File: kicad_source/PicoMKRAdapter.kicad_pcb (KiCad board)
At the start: 2 copper layers, 51 x 27 mm, 5 parts, among them CN1 RASPBERRYPI_PICO, CN2 ARDUINO_MKR, CN3 CONN_01X04

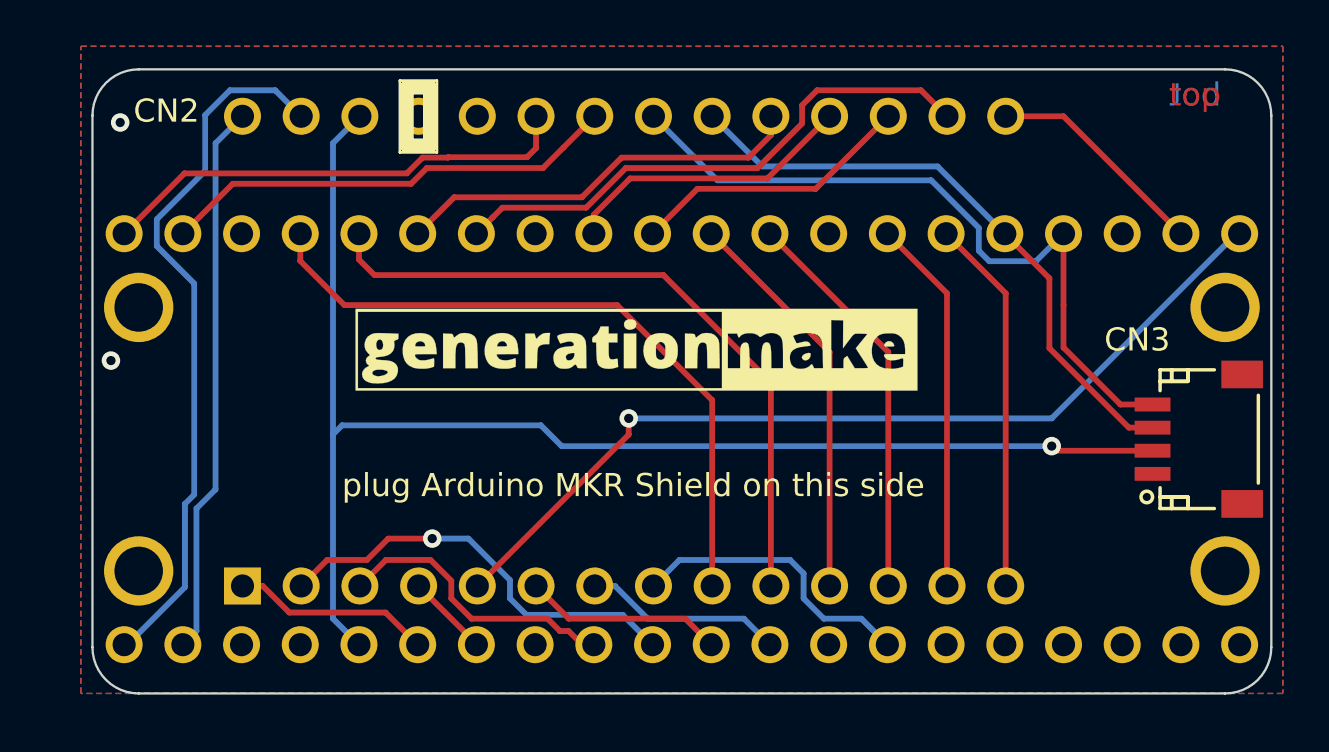
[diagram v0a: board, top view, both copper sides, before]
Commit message: updated layout and schematic, added i2c and serial connectors
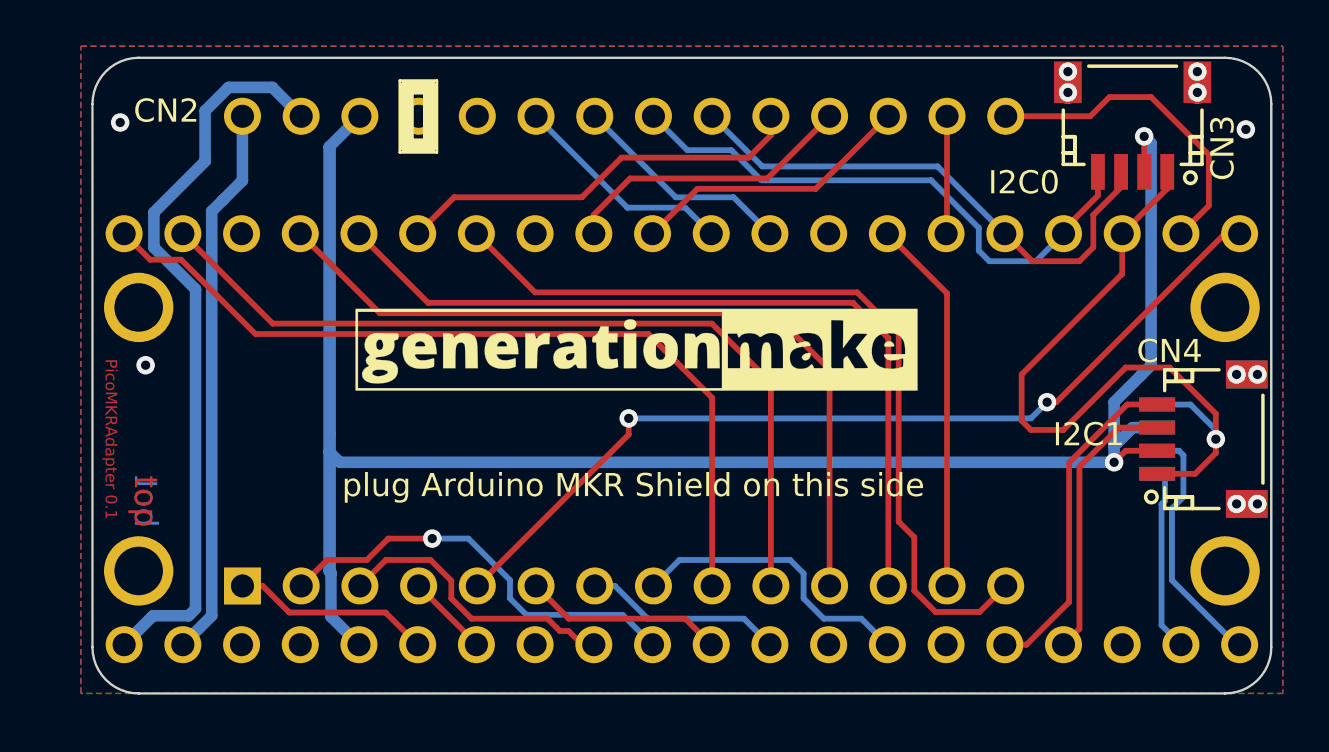
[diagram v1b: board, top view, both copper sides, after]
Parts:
- added CN4: CONN_01X04, connectors_JST_SH:Connectors_JST_SM04B-SRSS-TB, F.Cu at (202.5, 100.0)
- added CN5: CONN_01X04, connectors_JST_SH:Connectors_JST_SM04B-SRSS-TB, B.Cu at (202.5, 100.0)
- moved CN3 13.8 mm to (199.5, 86.5), turned to 180 degrees
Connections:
- net /SCL renamed /I2C0_SCL
- net /SDA renamed /I2C0_SDA
- CN1 pad 1: /TX -> /0
- CN1 pad 11: /2 -> /UART1_TX
- CN1 pad 12: /3 -> /UART1_RX
- CN1 pad 15: /5 -> /7
- CN1 pad 2: /RX -> /1
- CN1 pad 21: (no net) -> /UART0_TX
- CN1 pad 22: (no net) -> /UART0_RX
- CN1 pad 24: (no net) -> /I2C1_SDA
- CN1 pad 25: (no net) -> /I2C1_SCL
- CN1 pad 4: /0 -> /2
- CN1 pad 5: /1 -> /3
- CN1 pad 7: /7 -> /5
- CN2 pad 22: /RX -> /UART1_RX
- CN2 pad 23: /TX -> /UART1_TX
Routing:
- net +3V3: track 59.9 -> 102.6 mm, vias 1 -> 2
- net GND: track 0.00 -> 31.9 mm, vias 2 -> 4
- net /TX: track 20.7 -> 0.00 mm
- net /5: track 16.3 -> 36.3 mm
- net /RX: track 19.9 -> 0.00 mm
- net /7: track 23.9 -> 5.10 mm
- net /3: track 17.4 -> 35.5 mm
- net /2: track 17.4 -> 34.7 mm
- net /I2C1_SCL: track 0.00 -> 14.4 mm
- net /I2C1_SDA: track 0.00 -> 12.0 mm
- net /UART0_TX: track 0.00 -> 10.9 mm
- net /UART1_TX: track 0.00 -> 9.68 mm
- net /UART1_RX: track 0.00 -> 9.68 mm
- net /UART0_RX: track 0.00 -> 8.14 mm
- net /0: track 29.5 -> 36.5 mm
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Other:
- board size 51 x 27 mm -> 51 x 27.5 mm
- board text added: "I2C0"
- board text added: "I2C1"
- board text added: "PicoMKRAdapter 0.1"
- board text added: "UART0"

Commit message: updated pico footprint
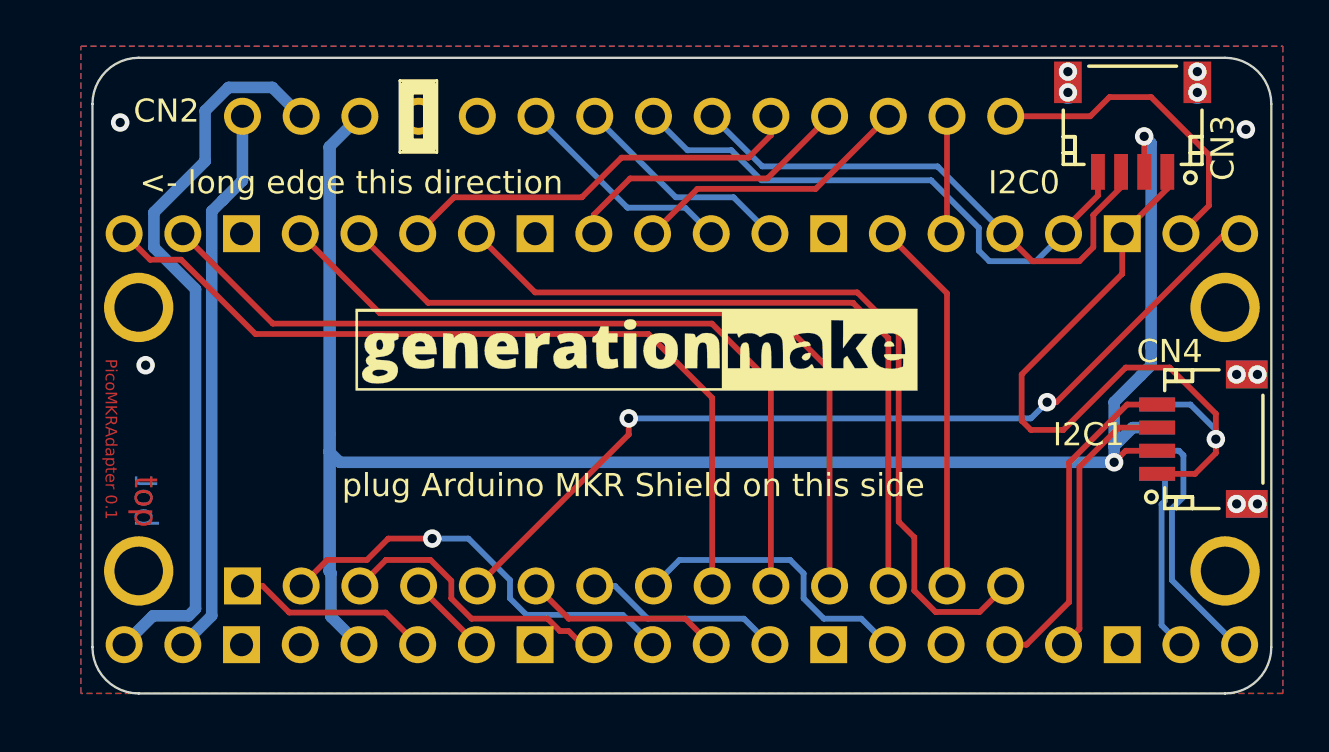
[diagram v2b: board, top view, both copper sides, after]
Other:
- board text added: "<- long edge this direction"
- board text added: "plug Rasperry Pi Pico on this side USB this direction ->"
- board text removed: "plug Rasperry Pi Pico on this side"

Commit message: connected RUN to RESET, added some labels
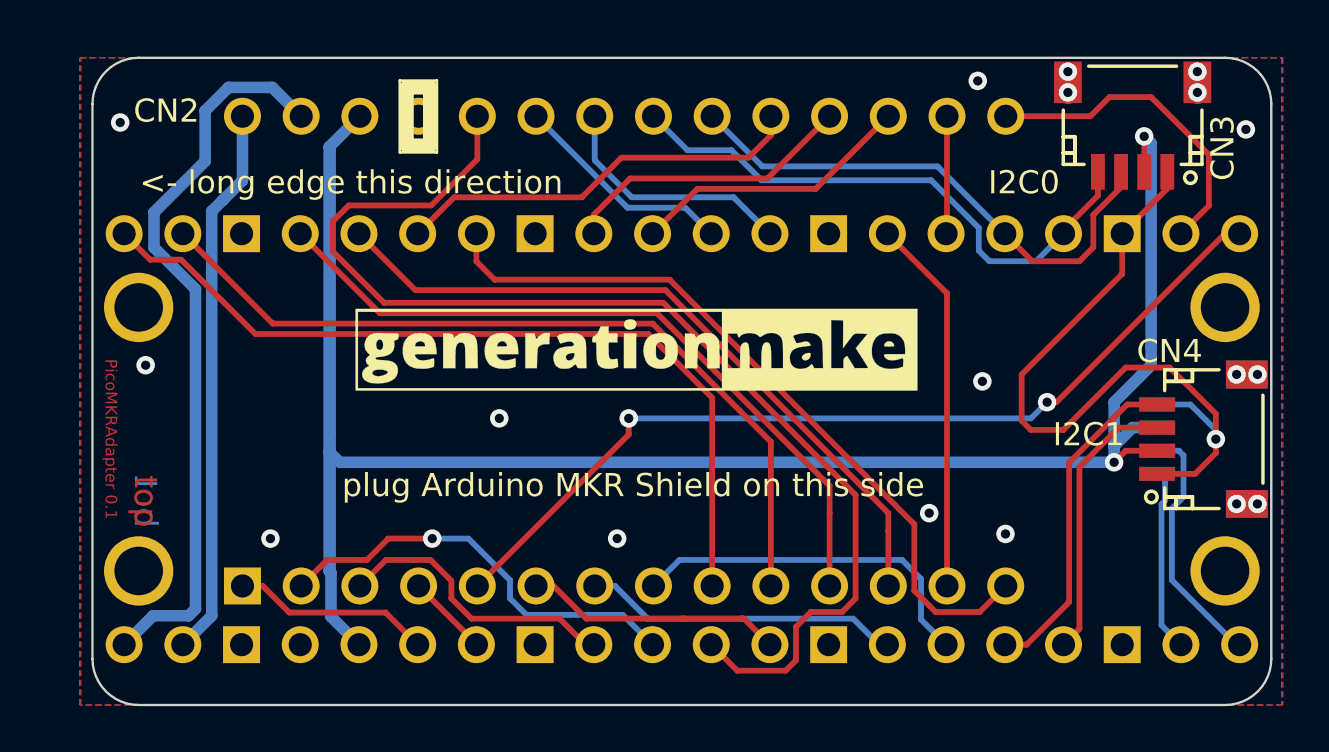
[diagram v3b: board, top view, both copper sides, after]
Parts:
- added L3: Label, Symbol:OSHW-Symbol_6.7x6mm_SilkScreen, B.Cu at (161.6, 95.8)
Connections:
- CN1 pad 26: (no net) -> /A6
- CN1 pad 27: /A6 -> /A5
- CN1 pad 29: /A5 -> /A4
- CN1 pad 30: /A4 -> /RESET
- CN2 pad 24: (no net) -> /RESET
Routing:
- net /RESET: track 0.00 -> 50.8 mm
- net /A5: track 8.63 -> 13.9 mm
- net /3: track 35.5 -> 31.1 mm
- net /5: track 36.3 -> 32.5 mm
- net /2: track 34.7 -> 31.8 mm
- net /A6: track 12.7 -> 15.7 mm
- net /A4: track 8.63 -> 11.4 mm
- net /1: track 36.9 -> 35.4 mm
- net /UART1_RX: track 9.68 -> 10.8 mm
- net GND: vias 4 -> 11
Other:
- board size 51 x 27.5 mm -> 51 x 28 mm
- board text added: "licensed under CERN OHL v.1.2"

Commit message: updated pdfs and images
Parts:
- CN3, CN4, CN5: value CONN_01X04 -> SM04B-SRSS-TB
